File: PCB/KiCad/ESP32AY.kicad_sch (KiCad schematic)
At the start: 106 parts, among them J1 USB_C_Receptacle_USB2.0_14P, J2 MiniJack, J3 SD Card, Q1 BC807, Q2 BC817, Q3 BC817, SW1 Check bat, SW2 EN, SW3 BOOT, U1 AY-3-8910, U2 AY-3-8910, U3 CH340G, U4 ESP32-WROOM-32, U5 TPA6130A2RTJTG4, U6 IP5306, U7 AMS1117-3.3, U8 74HC595, U9 74HC595, Y3 12MHz

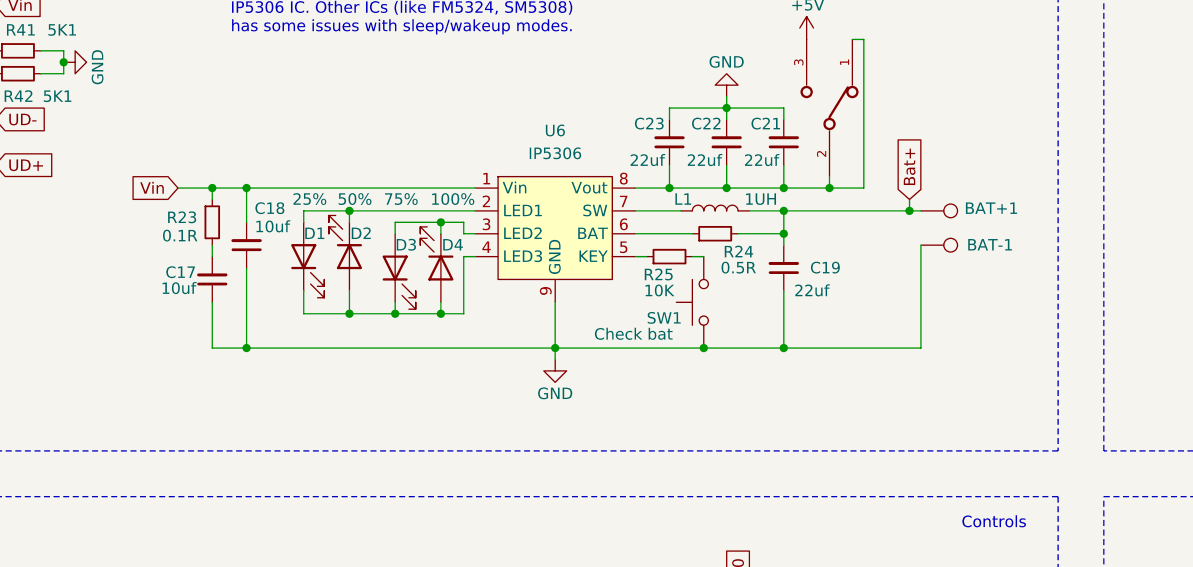
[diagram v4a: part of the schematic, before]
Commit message: Added C30 to the charger unit
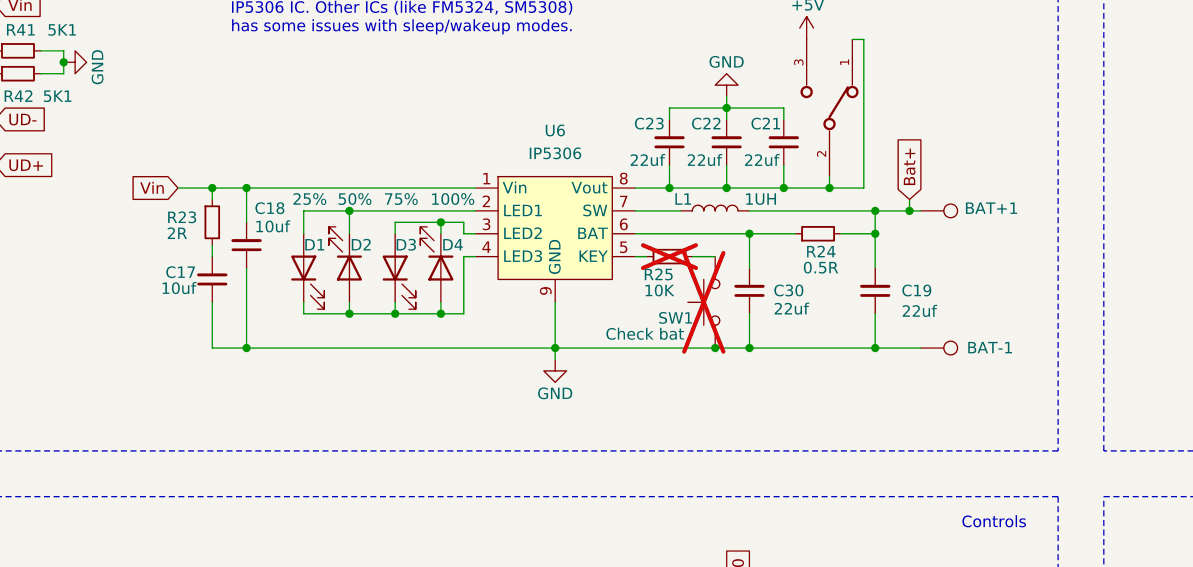
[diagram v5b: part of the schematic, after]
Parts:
- added C30: 22uf, Capacitor_SMD:C_0805_2012Metric_Pad1.18x1.45mm_HandSolder, symbol Device:C_Small
- BAT+1, BAT-1: now left out of the parts list
- R23: value 0.1R -> 2R
- R25, SW1: now not fitted; now left out of the parts list
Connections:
- net GND: now also C30.1
- net at R24.1, U6.6 (BAT): now also C30.2
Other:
- moved on the sheet: BAT-1, C19, D1, D2, R24

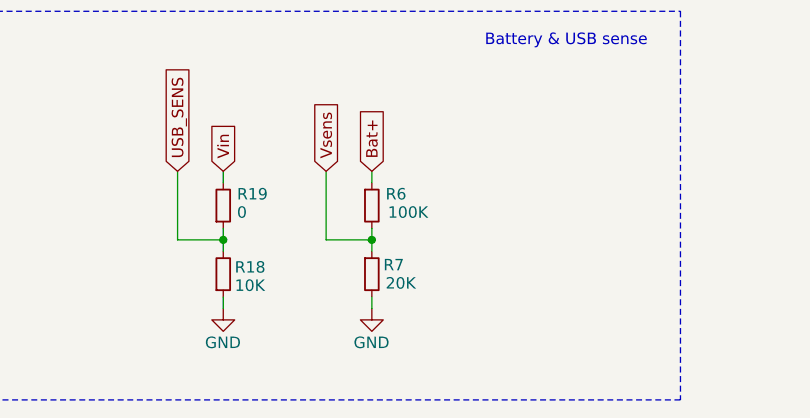
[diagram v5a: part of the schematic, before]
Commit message: Fixed R7 from 20k to 10k
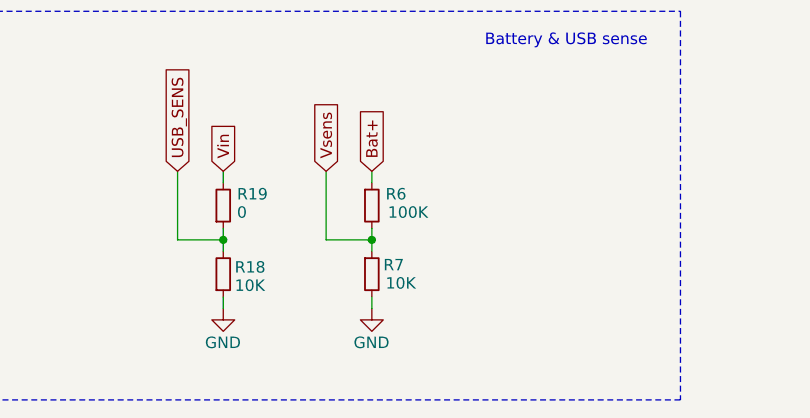
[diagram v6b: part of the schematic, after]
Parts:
- R7: value 20K -> 10K
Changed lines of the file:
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@@
 			)
 		)
-		(property "Value" "20K"
+		(property "Value" "10K"
 			(at 141.224 267.716 0)
 			(effects

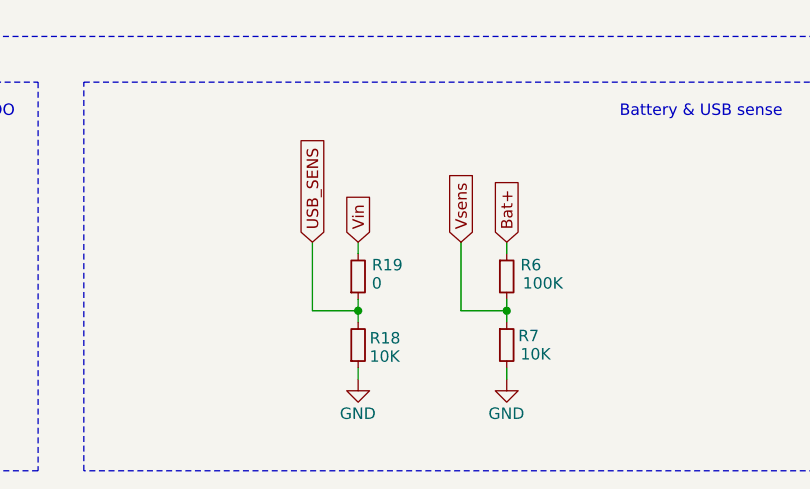
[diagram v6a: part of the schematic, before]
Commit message: Schematics change: replaced R19 from 0 to 8K2
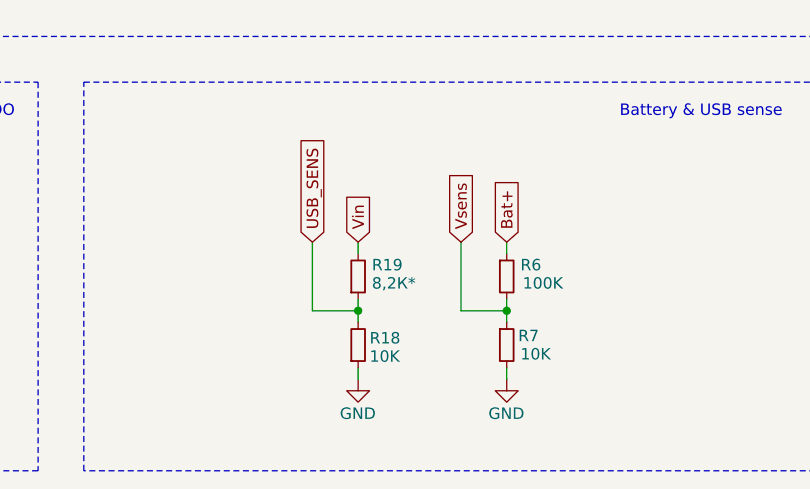
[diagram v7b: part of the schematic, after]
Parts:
- R19: value 0 -> 8,2К*
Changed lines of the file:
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@@
 			)
 		)
-		(property "Value" "0"
+		(property "Value" "8,2К*"
 			(at 124.714 259.842 0)
 			(effects

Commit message: RevC1 - initial commit
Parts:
- added C35, C36: 100n, Capacitor_SMD:C_0805_2012Metric_Pad1.18x1.45mm_HandSolder, symbol Device:C_Small
- added U10: DS3231MZ, Package_SO:SOIC-8_3.9x4.9mm_P1.27mm, symbol Timer_RTC:DS3231MZ
- added U11: MB85RC256V, Package_SO:SOIC-8_3.9x4.9mm_P1.27mm, symbol Memory_EEPROM:24LC256
- C19, C21, C22, C30: footprint Capacitor_SMD:C_0805_2012Metric_Pad1.18x1.45mm_HandSolder -> Capacitor_SMD:C_1206_3216Metric_Pad1.33x1.80mm_HandSolder
- C23: footprint Capacitor_SMD:C_0805_2012Metric -> Capacitor_SMD:C_1206_3216Metric_Pad1.33x1.80mm_HandSolder
- C33, C34, Y3: now not fitted; now left out of the parts list
- R23: footprint Resistor_SMD:R_0805_2012Metric -> Resistor_SMD:R_0805_2012Metric_Pad1.20x1.40mm_HandSolder
- U3: value CH340G -> CH340C
- U8, U9: footprint Package_SO:SO-16_5.3x10.2mm_P1.27mm -> Package_SO:SO-16_3.9x9.9mm_P1.27mm
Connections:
- net +3.3V: now also C35.1, C36.1, U10.2 (VCC), U11.8 (VCC)
- net Bat+: now also U10.6 (VBAT)
- net GND: now also C35.2, C36.2, U10.5 (GND), U11.1 (A0), U11.2 (A1), U11.3 (A2), U11.4 (GND), U11.7 (WP)
- net SCL: now also U10.7 (SDA), U11.6 (SCL)
- net SDA: now also U10.8 (SCL), U11.5 (SDA)
- no-connect marks 55 -> 58
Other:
- note added: "Please note: in case of using CH340G please populate Y3, C33, C34"
- note added: "RTC & FRAM"
- moved on the sheet: C24, C25, C28, C3, C4, J3, R18, R19, R29, R31, R6, R7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
